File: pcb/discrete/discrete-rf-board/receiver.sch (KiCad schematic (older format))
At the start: 0 parts

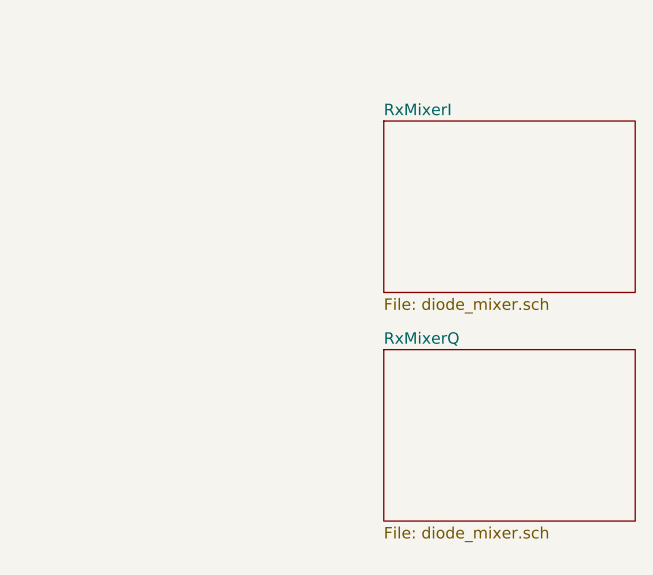
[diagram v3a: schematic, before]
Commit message: Capture IF amplifier stages and work on LNA stages
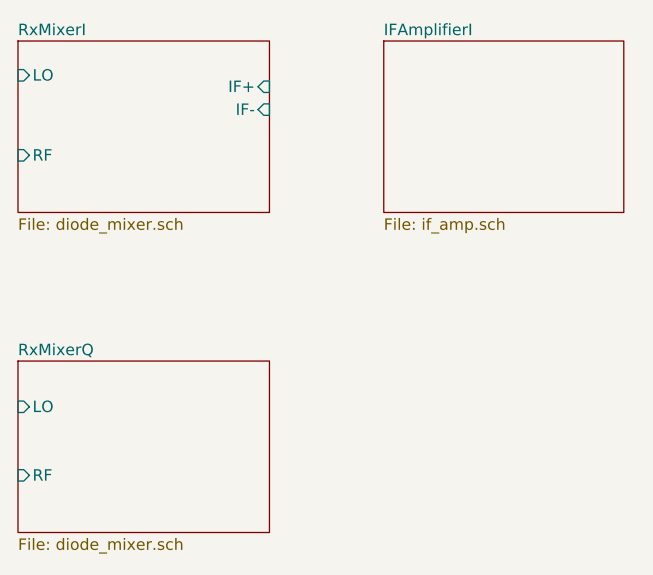
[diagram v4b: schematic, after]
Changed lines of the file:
@@
 $Descr A4 11693 8268
 encoding utf-8
-Sheet 3 8
+Sheet 2 9
 Title ""
 Date ""
@@
 $EndDescr
 $Sheet
-S 6500 2900 1100 750
+S 4900 2550 1100 750
 U 5CC1CC09
 F0 "RxMixerI" 50
 F1 "diode_mixer.sch" 50
+F2 "LO" I L 4900 2700 50
+F3 "RF" I L 4900 3050 50
+F4 "IF+" I R 6000 2750 50
+F5 "IF-" I R 6000 2850 50
 $EndSheet
 $Sheet
-S 6500 3900 1100 750
+S 6500 2550 1050 750
+U 5CC4DFC2
+F0 "IFAmplifierI" 50
+F1 "if_amp.sch" 50
+$EndSheet
+$Sheet
+S 4900 3950 1100 750
 U 5CC4015A
 F0 "RxMixerQ" 50
 F1 "diode_mixer.sch" 50
+F2 "LO" I L 4900 4150 50
+F3 "RF" I L 4900 4450 50
 $EndSheet
 $EndSCHEMATC

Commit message: Save changes while moving over to the new laptop
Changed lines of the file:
@@
 $Descr A4 11693 8268
 encoding utf-8
-Sheet 2 9
+Sheet 2 11
 Title ""
 Date ""
@@
 $EndSheet
 $Sheet
-S 6500 2550 1050 750
+S 6450 2400 1100 1000
 U 5CC4DFC2
 F0 "IFAmplifierI" 50
 F1 "if_amp.sch" 50
+F2 "+5V" I L 6450 2500 50
+F3 "IN+" I L 6450 2750 50
+F4 "IN-" I L 6450 2850 50
+F5 "BIAS" I L 6450 3250 50
+F6 "OUT+" I R 7550 2700 50
+F7 "OUT-" I R 7550 2800 50
+F8 "BYPASS1" I L 6450 3000 50
+F9 "BYPASS2" I L 6450 3100 50
 $EndSheet
 $Sheet
-S 4900 3950 1100 750
+S 4950 3850 1100 750
 U 5CC4015A
 F0 "RxMixerQ" 50
 F1 "diode_mixer.sch" 50
-F2 "LO" I L 4900 4150 50
-F3 "RF" I L 4900 4450 50
+F2 "LO" I L 4950 4050 50
+F3 "RF" I L 4950 4350 50
+F4 "IF+" I R 6050 4150 50
+F5 "IF-" I R 6050 4250 50
+$EndSheet
+$Sheet
+S 6450 3800 1100 1000
+U 5CC9409A
+F0 "sheet5CC94090" 50
+F1 "if_amp.sch" 50
+F2 "+5V" I L 6450 3900 50
+F3 "IN+" I L 6450 4150 50
+F4 "IN-" I L 6450 4250 50
+F5 "BIAS" I L 6450 4650 50
+F6 "OUT+" I R 7550 4100 50
+F7 "OUT-" I R 7550 4200 50
+F8 "BYPASS1" I L 6450 4400 50
+F9 "BYPASS2" I L 6450 4500 50
+$EndSheet
+$Sheet
+S 3350 3000 1200 1050
+U 5CE74EBE
+F0 "LNA" 50
+F1 "lna.sch" 50
 $EndSheet
 $EndSCHEMATC

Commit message: Merge stuff I guess, hopefully this doesn't break too much
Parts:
- added FL201: SF2098H, symbol discrete-parts:SF2098H
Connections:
- new net GND: FL201.2 (GND), FL201.4 (GND)
- new net LNA/OUT: FL201.1 (IN)
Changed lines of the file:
@@
 $EndSheet
 $Sheet
-S 3350 3000 1200 1050
+S 1150 3050 1200 1050
 U 5CE74EBE
 F0 "LNA" 50
 F1 "lna.sch" 50
+F2 "OUT" I R 2350 3550 50
+F3 "IN" I L 1150 3550 50
+F4 "+5V0" I L 1150 3200 50
+F5 "BYP1_3V3" I L 1150 3850 50
+F6 "BYP2_3V3" I L 1150 3950 50
 $EndSheet
+$Comp
+L discrete-parts:SF2098H FL201
+U 1 1 5D1C604E
+P 2900 3550
+F 0 "FL201" H 2650 3850 50  0000 C CNN
+F 1 "SF2098H" H 3150 3850 50  0000 C CNN
+F 2 "" H 2900 3100 50  0001 C CNN
+F 3 "" H 2900 3950 50  0001 C CNN
+	1    2900 3550
+	1    0    0    -1
+$EndComp
+$Comp
+L power:GND #PWR0201
+U 1 1 5D1C755D
+P 3100 4100
+F 0 "#PWR0201" H 3100 3850 50  0001 C CNN
+F 1 "GND" H 3100 3950 50  0000 C CNN
+F 2 "" H 3100 4100 50  0001 C CNN
+F 3 "" H 3100 4100 50  0001 C CNN
+	1    3100 4100
+	1    0    0    -1
+$EndComp
+Wire Wire Line
+	2700 3950 2700 4000
+Wire Wire Line
+	2700 4000 3100 4000
+Wire Wire Line
+	3100 4000 3100 3950
+Wire Wire Line
+	3100 4000 3100 4100
+Connection ~ 3100 4000
+Wire Wire Line
+	2350 3550 2500 3550
 $EndSCHEMATC
